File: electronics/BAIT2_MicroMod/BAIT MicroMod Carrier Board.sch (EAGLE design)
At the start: 152 parts, among them J1 SJ-43516-SMT, J10 QWIIC_RIGHT_ANGLE, J15 SM06B-SRSS-TB(LF)(SN), J2 ST-TF-003A, J4 JST_6_PIN_VERTICAL, J5 QWIIC_RIGHT_ANGLE, J6 JST 2PH, J7 MICROMOD-2222-C, SW1 SKQGADE010, SW2 SKQGADE010, U1 SGTL5000-32, U10 TSL25911, U2 AP7313, U3 3.3V, U4 3.3V, U5 BQ27441-G1, U6 BQ24074, U7 LoRa-E5-HF, U8 S-1172B33-E6T1U, U9 BOSCH_TOOLS_BME680BOSCH_TOOLS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

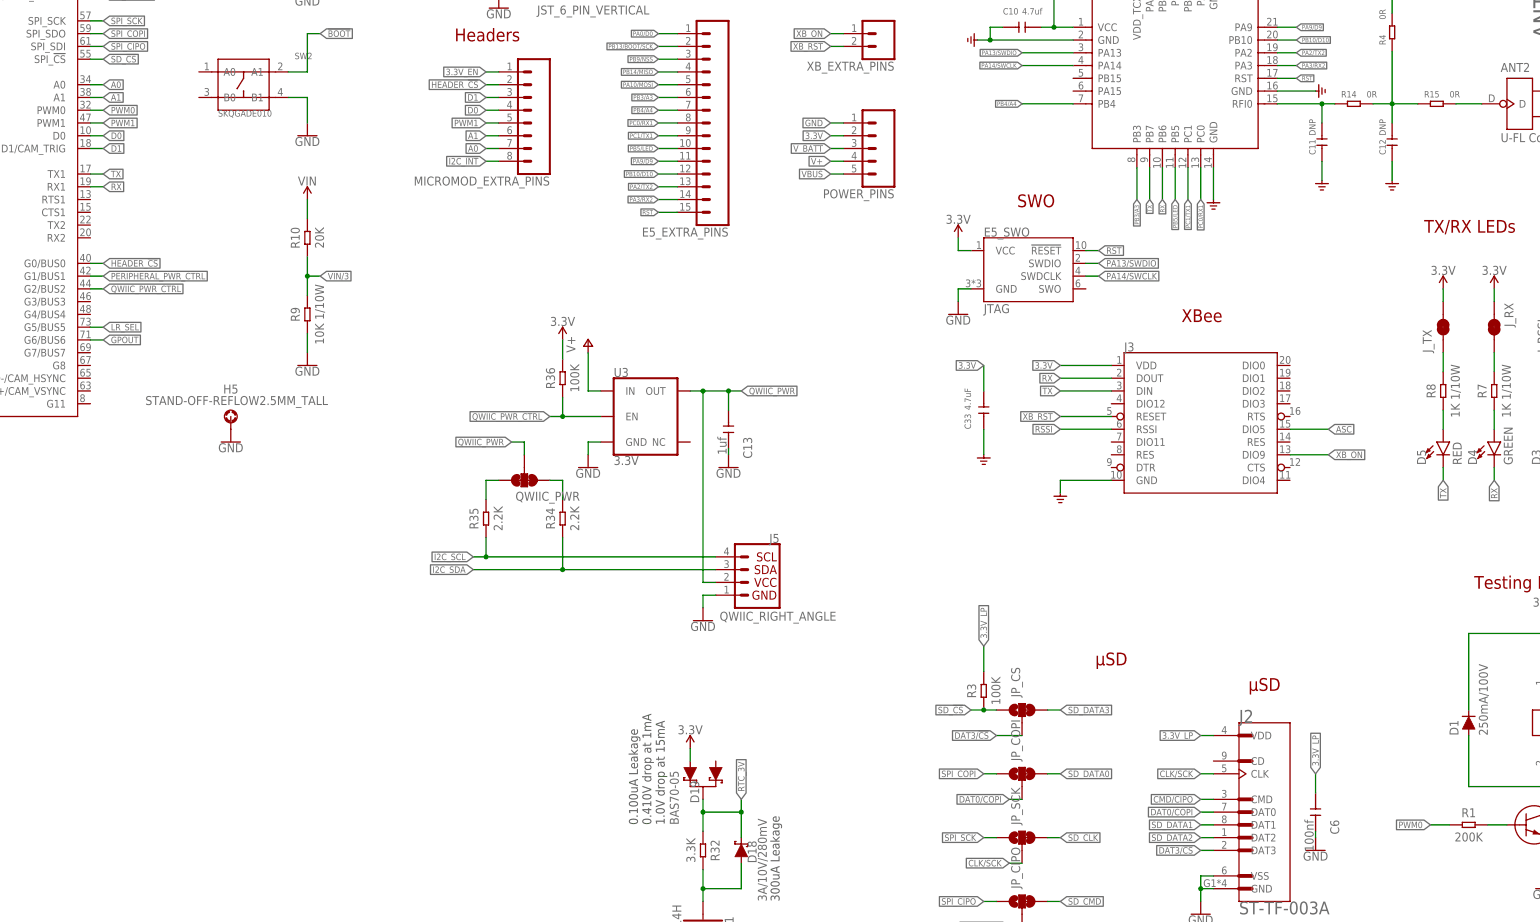
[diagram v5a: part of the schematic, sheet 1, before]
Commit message: Connect SGTL to I2S2 pins on micromod connector
Solves #6 in schematic, but creates #14
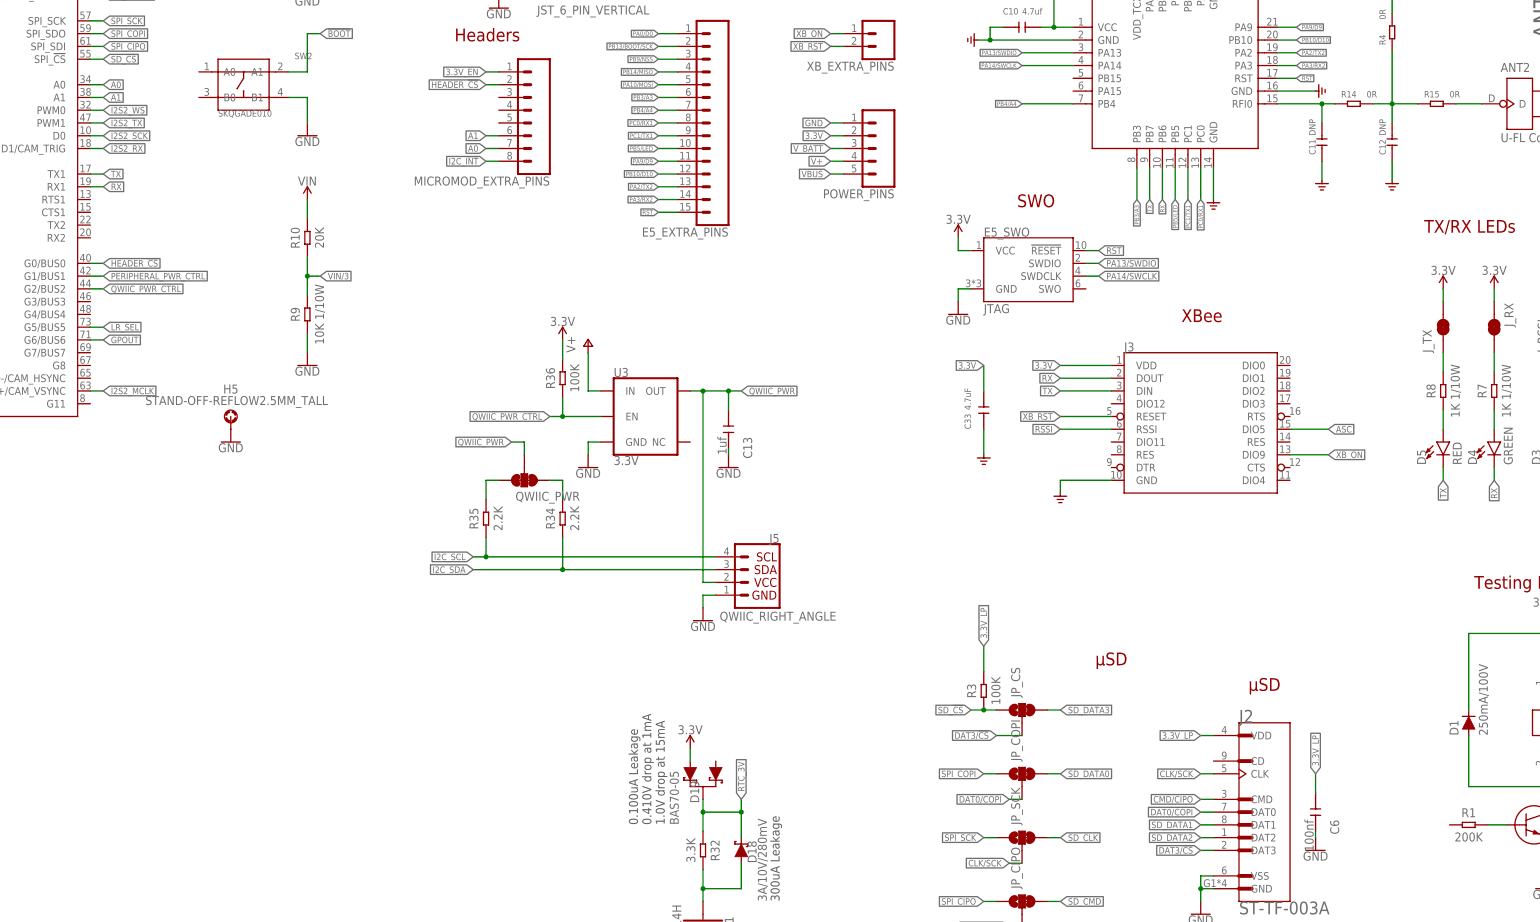
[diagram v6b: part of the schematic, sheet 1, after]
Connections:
- removed net D0: J7.D0, MICROMOD_EXTRA_PINS.4
- removed net D1: J7.D1/CAM_TRIG, MICROMOD_EXTRA_PINS.3
- removed net PWM0: J7.PWM0, R1.1
- removed net PWM1: J7.PWM1, MICROMOD_EXTRA_PINS.5
- new net I2S2_MCLK: J7.G10/ADC_D+/CAM_VSYNC, U1.SYS_MCLK
- new net I2S2_RX: J7.D1/CAM_TRIG, U1.I2S_DOUT
- new net I2S2_SCK: J7.D0, U1.I2S_SCLK
- new net I2S2_TX: J7.PWM1, U1.I2S_DIN
- new net I2S2_WS: J7.PWM0, U1.I2S_LRCLK
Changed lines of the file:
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@@
 </segment>
 </net>
-<net name="PWM0" class="0">
+<net name="I2S2_WS" class="0">
 <segment>
 <wire x1="71.12" y1="198.12" x2="73.66" y2="198.12" width="0.1524" layer="91" grouprefs="MICROMOD"/>
 <label x="73.66" y="198.12" size="1.27" layer="95" xref="yes" grouprefs="MICROMOD"/>
 <pinref part="J7" gate="J1" pin="PWM0"/>
-</segment>
-<segment>
-<pinref part="R1" gate="G$1" pin="1"/>
-<wire x1="341.63" y1="55.88" x2="337.82" y2="55.88" width="0.1524" layer="91" grouprefs="TESTING"/>
-<label x="337.82" y="55.88" size="1.27" layer="95" rot="R180" xref="yes" grouprefs="TESTING"/>
-</segment>
-</net>
-<net name="PWM1" class="0">
-<segment>
-<wire x1="71.12" y1="195.58" x2="73.66" y2="195.58" width="0.1524" layer="91" grouprefs="MICROMOD"/>
-<label x="73.66" y="195.58" size="1.27" layer="95" xref="yes" grouprefs="MICROMOD"/>
-<pinref part="J7" gate="J1" pin="PWM1"/>
-</segment>
-<segment>
-<wire x1="152.4" y1="195.58" x2="149.86" y2="195.58" width="0.1524" layer="91" grouprefs="PORTS"/>
-<label x="149.86" y="195.58" size="1.27" layer="95" rot="R180" xref="yes" grouprefs="PORTS"/>
-<pinref part="MICROMOD_EXTRA_PINS" gate="G$1" pin="5"/>
-</segment>
-</net>
-<net name="D0" class="0">
-<segment>
-<wire x1="71.12" y1="193.04" x2="73.66" y2="193.04" width="0.1524" layer="91" grouprefs="MICROMOD"/>
-<label x="73.66" y="193.04" size="1.27" layer="95" xref="yes" grouprefs="MICROMOD"/>
-<pinref part="J7" gate="J1" pin="D0"/>
-</segment>
-<segment>
-<wire x1="152.4" y1="198.12" x2="149.86" y2="198.12" width="0.1524" layer="91" grouprefs="PORTS"/>
-<label x="149.86" y="198.12" size="1.27" layer="95" rot="R180" xref="yes" grouprefs="PORTS"/>
-<pinref part="MICROMOD_EXTRA_PINS" gate="G$1" pin="4"/>
-</segment>
-</net>
-<net name="D1" class="0">
-<segment>
-<wire x1="71.12" y1="190.5" x2="73.66" y2="190.5" width="0.1524" layer="91" grouprefs="MICROMOD"/>
-<label x="73.66" y="190.5" size="1.27" layer="95" xref="yes" grouprefs="MICROMOD"/>
-<pinref part="J7" gate="J1" pin="D1/CAM_TRIG"/>
-</segment>
-<segment>
-<wire x1="152.4" y1="200.66" x2="149.86" y2="200.66" width="0.1524" layer="91" grouprefs="PORTS"/>
-<label x="149.86" y="200.66" size="1.27" layer="95" rot="R180" xref="yes" grouprefs="PORTS"/>
-<pinref part="MICROMOD_EXTRA_PINS" gate="G$1" pin="3"/>
 </segment>
 </net>
@@
 <wire x1="71.12" y1="152.4" x2="73.66" y2="152.4" width="0.1524" layer="91"/>
 <label x="73.66" y="152.4" size="1.27" layer="95" xref="yes"/>
+</segment>
+</net>
+<net name="I2S2_TX" class="0">
+<segment>
+<wire x1="71.12" y1="195.58" x2="73.66" y2="195.58" width="0.1524" layer="91" grouprefs="MICROMOD"/>
+<label x="73.66" y="195.58" size="1.27" layer="95" xref="yes" grouprefs="MICROMOD"/>
+<pinref part="J7" gate="J1" pin="PWM1"/>
+</segment>
+</net>
+<net name="I2S2_SCK" class="0">
+<segment>
+<wire x1="71.12" y1="193.04" x2="73.66" y2="193.04" width="0.1524" layer="91" grouprefs="MICROMOD"/>
+<label x="73.66" y="193.04" size="1.27" layer="95" xref="yes" grouprefs="MICROMOD"/>
+<pinref part="J7" gate="J1" pin="D0"/>
+</segment>
+</net>
+<net name="I2S2_RX" class="0">
+<segment>
+<wire x1="71.12" y1="190.5" x2="73.66" y2="190.5" width="0.1524" layer="91" grouprefs="MICROMOD"/>
+<label x="73.66" y="190.5" size="1.27" layer="95" xref="yes" grouprefs="MICROMOD"/>
+<pinref part="J7" gate="J1" pin="D1/CAM_TRIG"/>
+</segment>
+</net>
+<net name="I2S2_MCLK" class="0">
+<segment>
+<pinref part="J7" gate="J1" pin="G10/ADC_D+/CAM_VSYNC"/>
+<wire x1="71.12" y1="142.24" x2="73.66" y2="142.24" width="0.1524" layer="91"/>
+<label x="73.66" y="142.24" size="1.27" layer="95" xref="yes"/>
 </segment>
 </net>
@@
 </segment>
 </net>
+<net name="I2S2_MCLK" class="0">
+<segment>
+<pinref part="U1" gate="G$1" pin="SYS_MCLK"/>
+<wire x1="342.9" y1="198.12" x2="347.98" y2="198.12" width="0.1524" layer="91"/>
+<label x="347.98" y="198.12" size="1.27" layer="95" xref="yes"/>
+</segment>
+</net>
+<net name="I2S2_WS" class="0">
+<segment>
+<pinref part="U1" gate="G$1" pin="I2S_LRCLK"/>
+<wire x1="342.9" y1="194.31" x2="347.98" y2="194.31" width="0.1524" layer="91"/>
+<label x="347.98" y="194.31" size="1.27" layer="95" xref="yes"/>
+</segment>
+</net>
+<net name="I2S2_SCK" class="0">
+<segment>
+<pinref part="U1" gate="G$1" pin="I2S_SCLK"/>
+<wire x1="342.9" y1="191.77" x2="347.98" y2="191.77" width="0.1524" layer="91"/>
+<label x="347.98" y="191.77" size="1.27" layer="95" xref="yes"/>
+</segment>
+</net>
+<net name="I2S2_RX" class="0">
+<segment>
+<pinref part="U1" gate="G$1" pin="I2S_DOUT"/>
+<wire x1="342.9" y1="189.23" x2="347.98" y2="189.23" width="0.1524" layer="91"/>
+<label x="347.98" y="189.23" size="1.27" layer="95" xref="yes"/>
+</segment>
+</net>
+<net name="I2S2_TX" class="0">
+<segment>
+<pinref part="U1" gate="G$1" pin="I2S_DIN"/>
+<wire x1="342.9" y1="186.69" x2="347.98" y2="186.69" width="0.1524" layer="91"/>
+<label x="347.98" y="186.69" size="1.27" layer="95" xref="yes"/>
+</segment>
+</net>

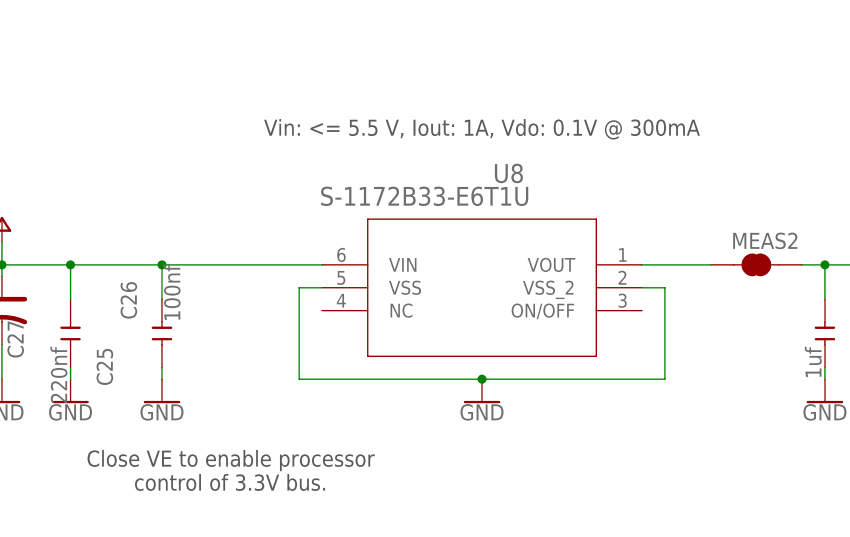
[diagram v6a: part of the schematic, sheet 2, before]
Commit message: Fixes enable issue with main 3.3V regulator
Resolves #3 in schematic and board
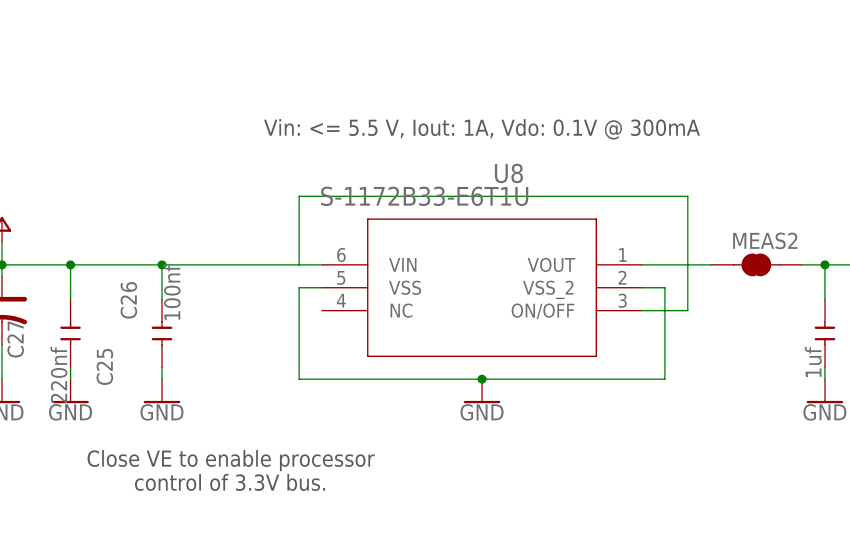
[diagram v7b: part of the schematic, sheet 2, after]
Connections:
- net V+: now also U8.ON/OFF
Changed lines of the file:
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@@
 <pinref part="U8" gate="A" pin="VIN"/>
 <wire x1="15.24" y1="223.52" x2="15.24" y2="226.06" width="0.1524" layer="91"/>
-<wire x1="33.02" y1="223.52" x2="50.8" y2="223.52" width="0.1524" layer="91"/>
+<wire x1="33.02" y1="223.52" x2="48.26" y2="223.52" width="0.1524" layer="91"/>
 <junction x="15.24" y="223.52"/>
 <junction x="22.86" y="223.52"/>
 <junction x="33.02" y="223.52"/>
+<wire x1="48.26" y1="223.52" x2="50.8" y2="223.52" width="0.1524" layer="91"/>
+<wire x1="48.26" y1="223.52" x2="48.26" y2="231.14" width="0.1524" layer="91"/>
+<wire x1="48.26" y1="231.14" x2="91.44" y2="231.14" width="0.1524" layer="91"/>
+<wire x1="91.44" y1="231.14" x2="91.44" y2="218.44" width="0.1524" layer="91"/>
+<pinref part="U8" gate="A" pin="ON/OFF"/>
+<wire x1="91.44" y1="218.44" x2="86.36" y2="218.44" width="0.1524" layer="91"/>
 </segment>
 </net>
